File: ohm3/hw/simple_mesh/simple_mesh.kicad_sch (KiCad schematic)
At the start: 21 parts, among them IC1 RaspberryPi_Pico, IC2 SX1262, J3 Conn_01x04, J4 Conn_01x04

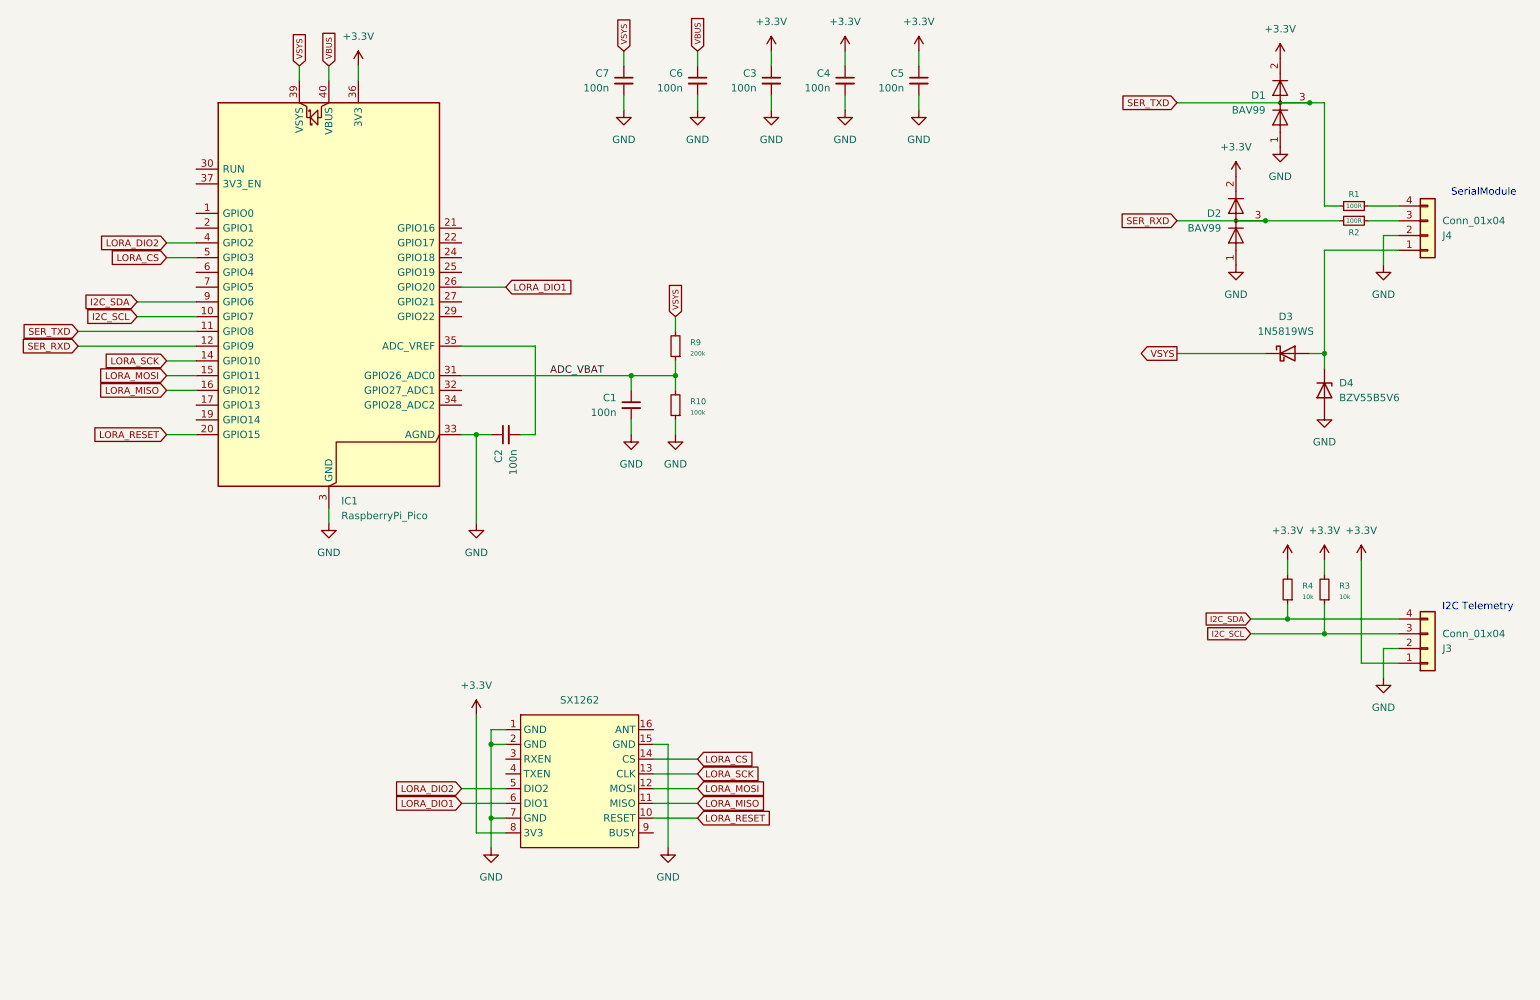
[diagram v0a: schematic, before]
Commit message: BUG - need to connect BUSY to DI02
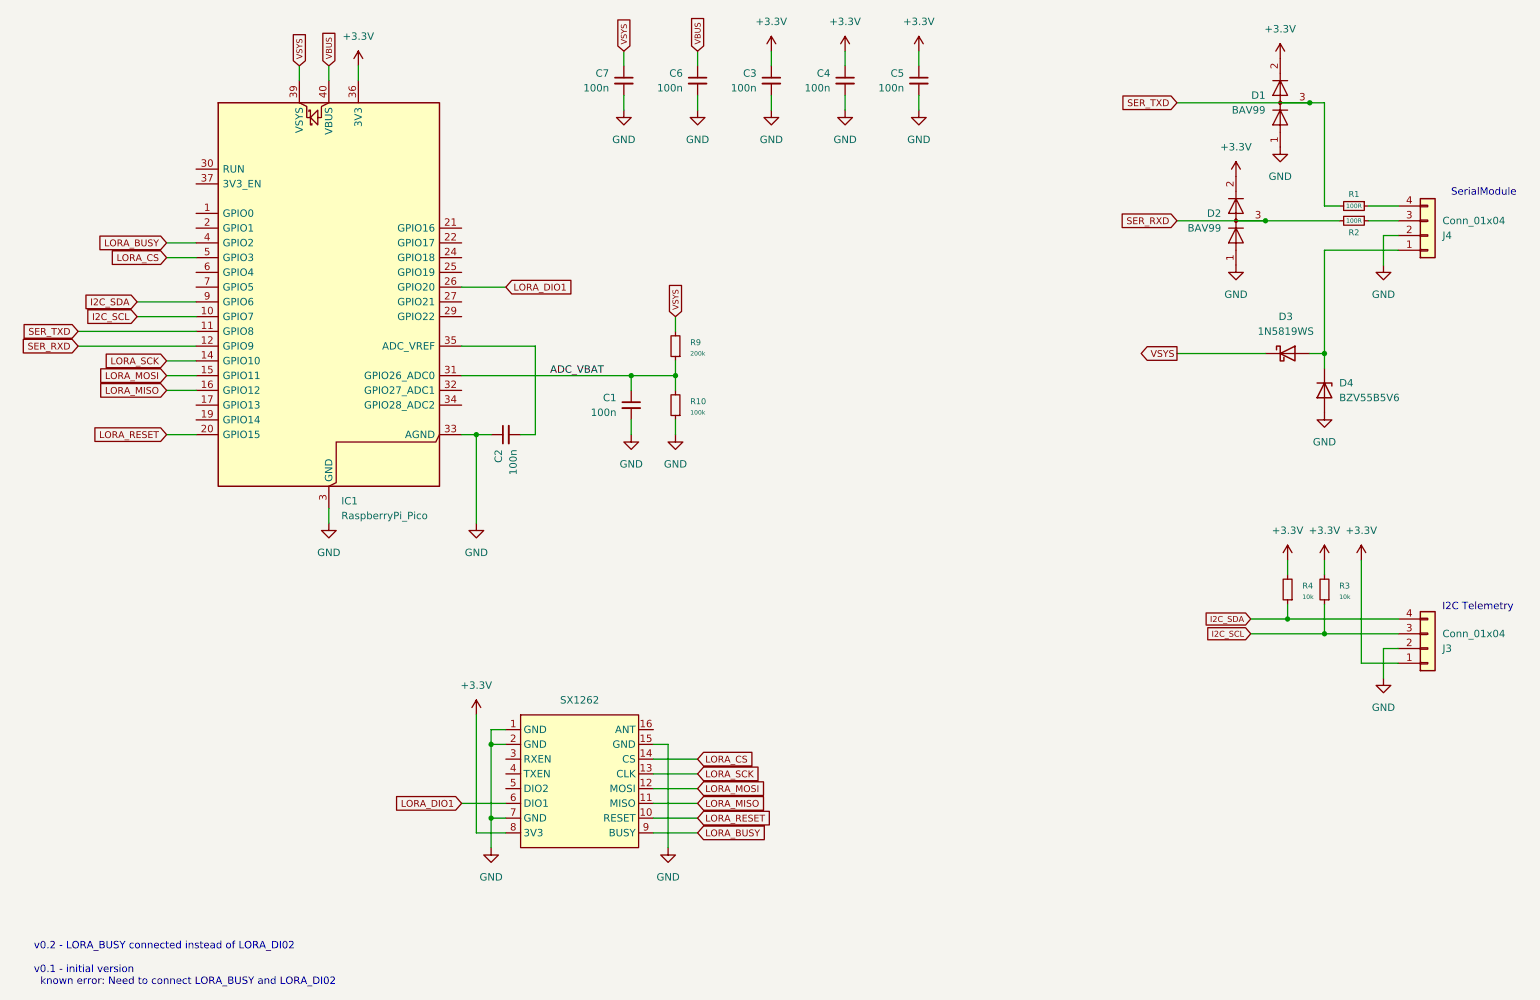
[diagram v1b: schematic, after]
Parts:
- D4: footprint Diode_SMD:D_SOD-123F -> Diode_SMD:D_SMA
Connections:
- net LORA_BUSY: now reaches IC2.9 (BUSY)
- net LORA_BUSY: now also IC1.4 (GPIO2)
- net LORA_DIO2: no longer names the net of IC2.5 (DIO2)
- net LORA_DIO2: no longer IC1.4 (GPIO2)
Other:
- note added: "v0.2 - LORA_BUSY connected instead of LORA_DI02 v0.1 - initial version known error: Need to connect LORA_BUSY and LORA_DI02"
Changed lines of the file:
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@@
 	(generator_version "9.0")
 	(paper "A4")
+	(text "v0.2 - LORA_BUSY connected instead of LORA_DI02\n\nv0.1 - initial version\n  known error: Need to connect LORA_BUSY and LORA_DI02"
+		(exclude_from_sim no)
+		(at 19.05 186.436 0)
+		(effects
+			(font
+				(size 1.27 1.27)
+			)
+			(justify left)
+		)
+	)
 	(text "I2C Telemetry"
 		(exclude_from_sim no)
@@
 	(wire
 		(pts
-			(xy 92.71 156.21) (xy 100.33 156.21)
-		)
-		(stroke
-			(width 0)
-			(type default)
-		)
-	)
-	(wire
-		(pts
 			(xy 36.83 72.39) (xy 46.99 72.39)
 		)
@@
 		(pts
 			(xy 248.92 55.88) (xy 254 55.88)
+		)
+		(stroke
+			(width 0)
+			(type default)
+		)
+	)
+	(wire
+		(pts
+			(xy 125.73 163.83) (xy 133.35 163.83)
 		)
 		(stroke
@@
 		)
 	)
-	(global_label "LORA_DIO2"
+	(global_label "LORA_BUSY"
 		(shape input)
 		(at 41.91 62.23 180)
@@
 		)
 		(property "Intersheetrefs" "${INTERSHEET_REFS}"
-			(at 29.872 62.23 0)
+			(at 29.4269 62.23 0)
 			(effects
 				(font
@@
 		)
 	)
-	(global_label "LORA_DIO2"
-		(shape input)
-		(at 92.71 156.21 180)
-		(fields_autoplaced yes)
-		(effects
-			(font
-				(size 1.1684 1.1684)
-			)
-			(justify right)
-		)
-		(property "Intersheetrefs" "${INTERSHEET_REFS}"
-			(at 80.672 156.21 0)
-			(effects
-				(font
-					(size 1.27 1.27)
-				)
-				(justify right)
-				(hide yes)
-			)
-		)
-	)
 	(global_label "VBUS"
 		(shape input)
@@
 		(property "Intersheetrefs" "${INTERSHEET_REFS}"
 			(at 69.85 25.4432 90)
+			(effects
+				(font
+					(size 1.27 1.27)
+				)
+				(justify left)
+				(hide yes)
+			)
+		)
+	)
+	(global_label "LORA_BUSY"
+		(shape input)
+		(at 133.35 163.83 0)
+		(fields_autoplaced yes)
+		(effects
+			(font
+				(size 1.1684 1.1684)
+			)
+			(justify left)
+		)
+		(property "Intersheetrefs" "${INTERSHEET_REFS}"
+			(at 145.8331 163.83 0)
 			(effects
 				(font
@@
 			)
 		)
-		(property "Footprint" "Diode_SMD:D_SOD-123F"
+		(property "Footprint" "Diode_SMD:D_SMA"
 			(at 236.855 87.63 0)
 			(effects
